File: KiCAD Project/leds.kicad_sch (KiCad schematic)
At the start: 192 parts

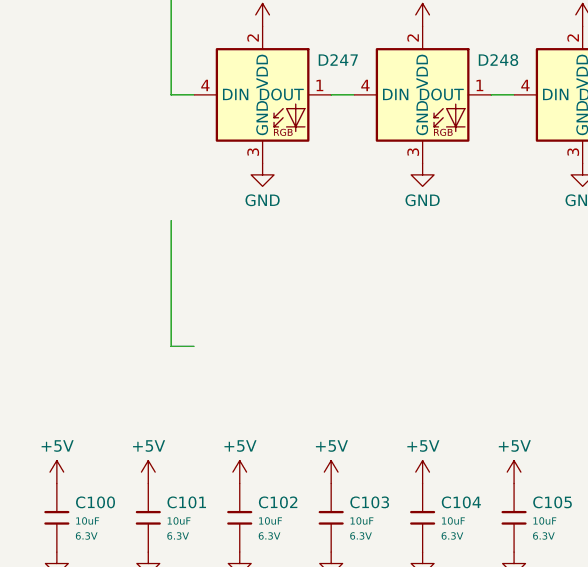
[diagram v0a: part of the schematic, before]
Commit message: Added annotations to schematic
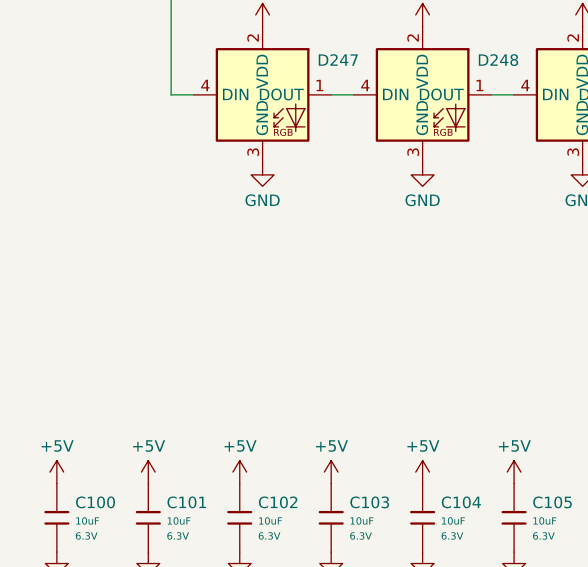
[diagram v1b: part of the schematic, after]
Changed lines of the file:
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@@
-	(wire
-		(pts
-			(xy 30.48 237.49) (xy 30.48 251.46)
-		)
-		(stroke
-			(width 0)
-			(type default)
-		)
-	)
-	(wire
-		(pts
-			(xy 30.48 251.46) (xy 33.02 251.46)
-		)
-		(stroke
-			(width 0)
-			(type default)
-		)
-	)
 	(wire
 		(pts
